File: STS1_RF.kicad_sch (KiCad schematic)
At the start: 6 parts, among them J1 Conn_Coaxial, J2 Conn_01x03_Male

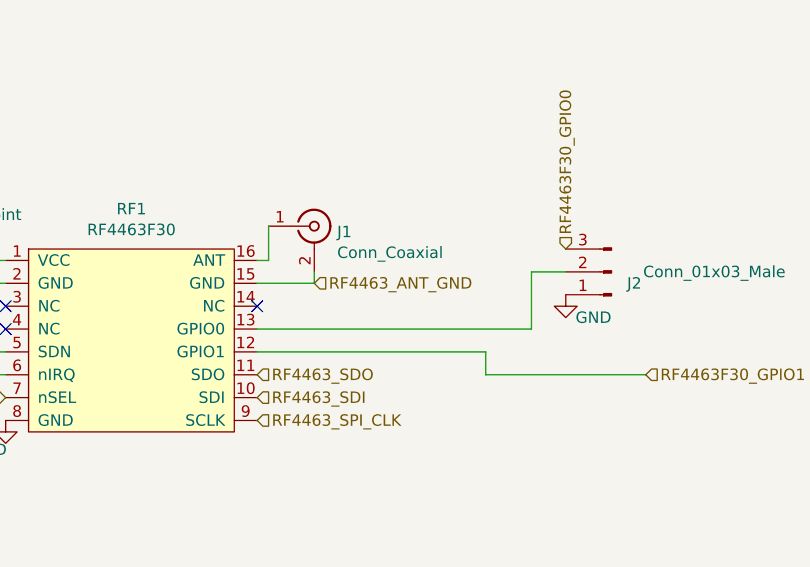
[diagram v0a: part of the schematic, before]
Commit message: more work done
All parts besides RF added
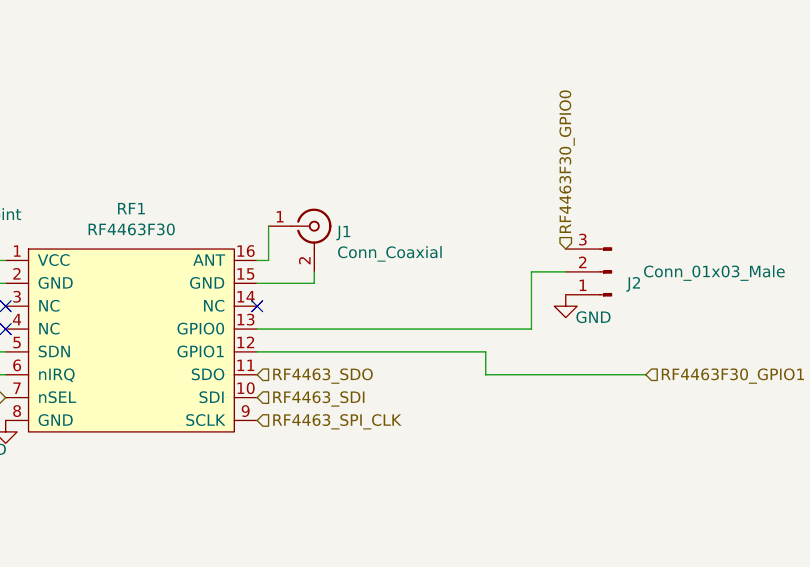
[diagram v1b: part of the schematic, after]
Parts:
- J1: footprint Connector_Coaxial:SMA_Amphenol_901-144_Vertical -> Connector_Coaxial:SMB_Jack_Vertical
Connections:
- net RF4463_ANT_GND: no longer names the net of J1.2 (Ext), RF1.15 (GND)
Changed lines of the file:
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@@
-    (effects (font (size 1.27 1.27)) (justify left))
-  )
-  (hierarchical_label "RF4463_ANT_GND" (shape input) (at 228.6 83.82 0)
     (effects (font (size 1.27 1.27)) (justify left))
   )
@@
       (effects (font (size 1.27 1.27)) (justify left))
     )
-    (property "Footprint" "Connector_Coaxial:SMA_Amphenol_901-144_Vertical" (id 2) (at 228.6 77.47 0)
+    (property "Footprint" "Connector_Coaxial:SMB_Jack_Vertical" (id 2) (at 228.6 77.47 0)
       (effects (font (size 1.27 1.27)) hide)
     )

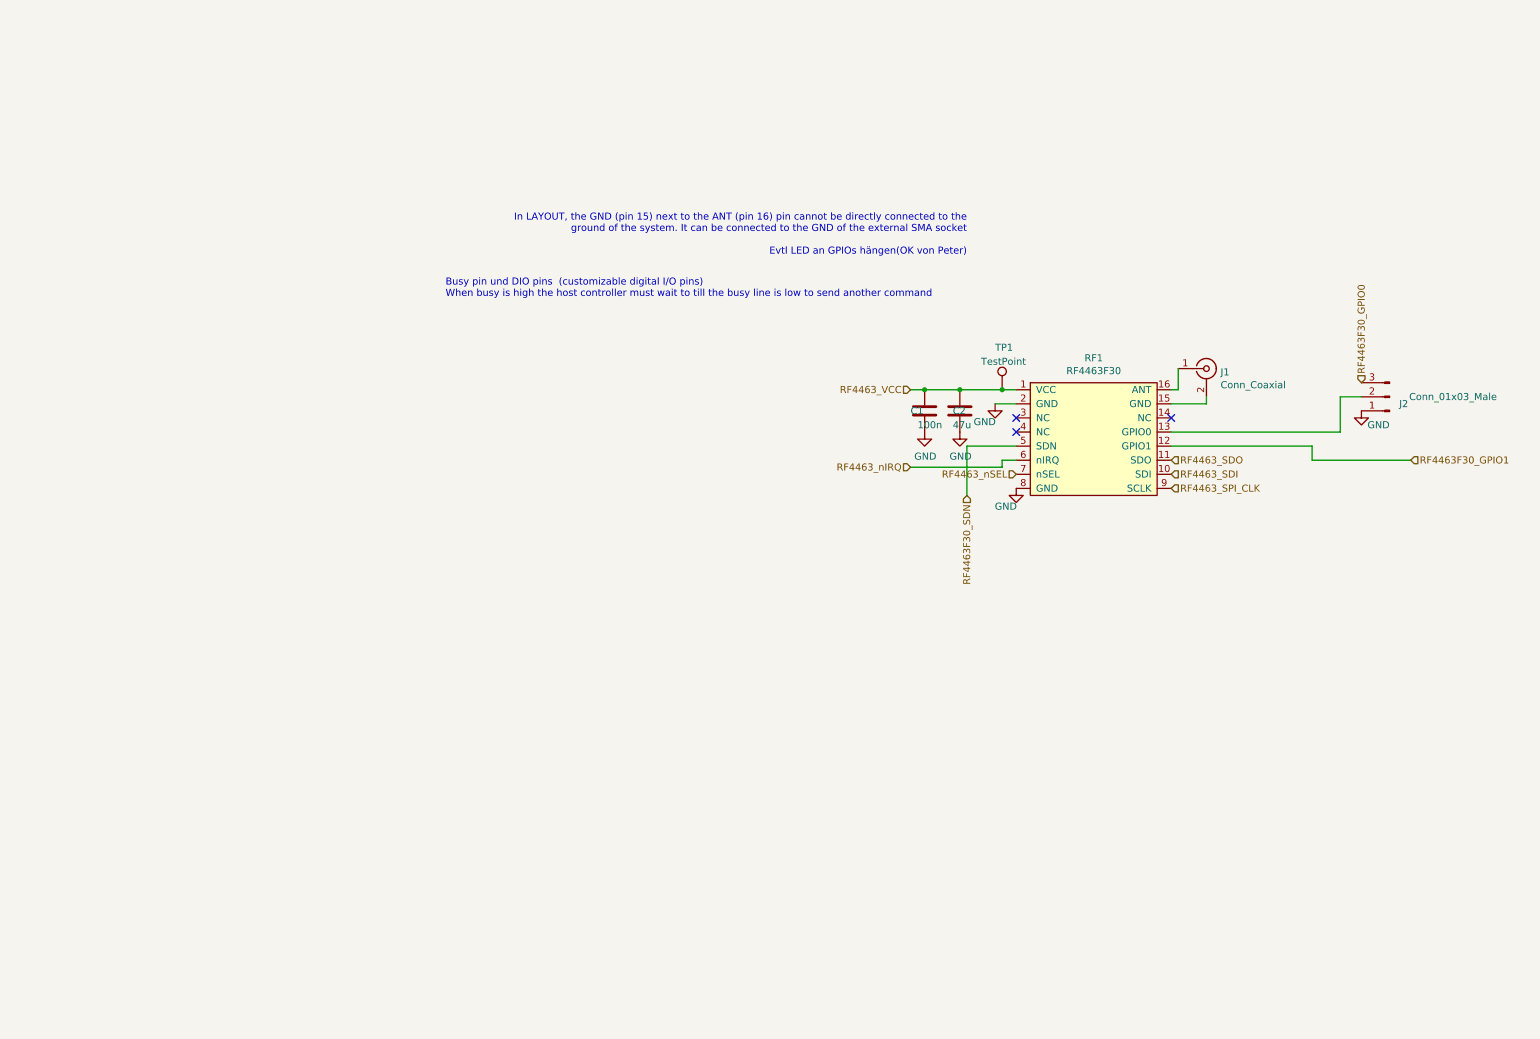
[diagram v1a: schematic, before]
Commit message: add RF part
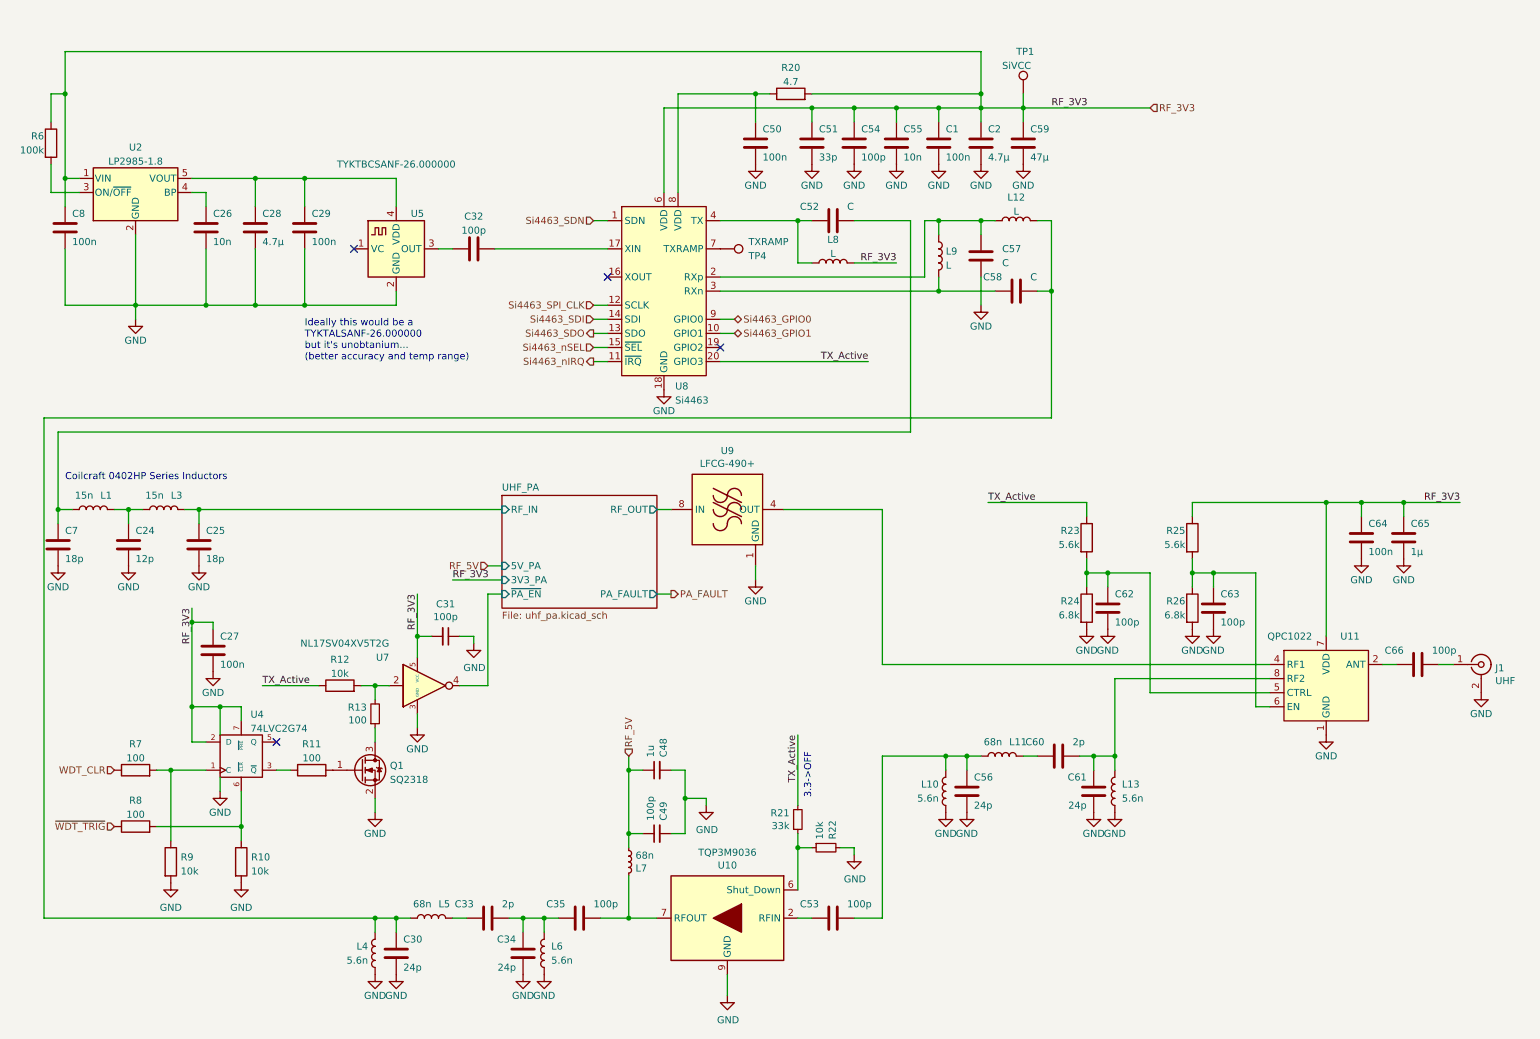
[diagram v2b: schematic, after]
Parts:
- removed J2: Conn_01x03_Male, STS1library:PinHeader_1x03_P2.54mm_Vertical_umdieEcke, symbol Connector:Conn_01x03_Male
- removed RF1: RF4463F30, STS1_RF:STS1_RF4463F30, symbol STS1_COBC_RFM:RF4463F30
- added C24: 12p, Capacitor_SMD:C_0402_1005Metric, symbol Device:C
- added C25, C7: 18p, Capacitor_SMD:C_0402_1005Metric, symbol Device:C
- added C26, C55: 10n, Capacitor_SMD:C_0805_2012Metric, symbol Device:C
- added C27, C29, C50, C64, C8: 100n, Capacitor_SMD:C_0805_2012Metric, symbol Device:C
- added C28: 4.7µ, Capacitor_SMD:C_0805_2012Metric, symbol Device:C
- added C30, C34, C56, C61: 24p, Capacitor_SMD:C_0402_1005Metric, symbol Device:C
- added C31, C49: 100p, Capacitor_SMD:C_0402_1005Metric, symbol Device:C_Small
- added C32, C35, C53, C54, C62, C63, C66: 100p, Capacitor_SMD:C_0402_1005Metric, symbol Device:C
- added C33, C60: 2p, Capacitor_SMD:C_0402_1005Metric, symbol Device:C
- added C48: 1u, Capacitor_SMD:C_0805_2012Metric, symbol Device:C_Small
- added C51: 33p, Capacitor_SMD:C_0402_1005Metric, symbol Device:C
- added C52, C57, C58: C, Capacitor_SMD:C_0402_1005Metric, symbol Device:C
- added C59: 47µ, Capacitor_SMD:C_0805_2012Metric, symbol Device:C
- added C65: 1µ, Capacitor_SMD:C_0805_2012Metric, symbol Device:C
- added L1, L3: 15n, Inductor_SMD:L_0402_1005Metric, symbol Device:L
- added L10, L13, L4, L6: 5.6n, Inductor_SMD:L_0402_1005Metric, symbol Device:L
- added L11, L5: 68n, Inductor_SMD:L_0402_1005Metric, symbol Device:L
- added L12, L8, L9: L, Inductor_SMD:L_0402_1005Metric, symbol Device:L
- added L7: 68n, Inductor_SMD:L_0402_1005Metric, symbol Device:L_Small
- added Q1: SQ2318, Package_TO_SOT_SMD:SOT-23, symbol Device:Q_NMOS_GSD
- added R10, R12, R9: 10k, Resistor_SMD:R_0603_1608Metric, symbol Device:R
- added R11, R7, R8: 100, Resistor_SMD:R_0603_1608Metric, symbol Device:R
- added R13: 100, Resistor_SMD:R_0603_1608Metric, symbol Device:R_Small
- added R20: 4.7, Resistor_SMD:R_0603_1608Metric, symbol Device:R
- added R21: 33k, Resistor_SMD:R_0603_1608Metric, symbol Device:R_Small
- added R22: 10k, Resistor_SMD:R_0603_1608Metric, symbol Device:R_Small
- added R23, R25: 5.6k, Resistor_SMD:R_0603_1608Metric, symbol Device:R
- added R24, R26: 6.8k, Resistor_SMD:R_0603_1608Metric, symbol Device:R
- added R6: 100k, Resistor_SMD:R_0603_1608Metric, symbol Device:R
- added TP4: TXRAMP, STS1library:STS1_Testpoint, symbol Connector:TestPoint
- added U10: TQP3M9036, lsf-kicad-lib:DFN-8-1EP_2x2mm_P0.5mm_EP0.7x1.6mm_ThermalVias, symbol lsf-kicad:TQP3M9036
- added U11: QPC1022, STS_Package_LGA:Qorvo_9Pin_1.1x1.5mm_LGA, symbol STS_RF_Module:QPC1022
- added U2: LP2985-1.8, Package_TO_SOT_SMD:SOT-23-5, symbol Regulator_Linear:LP2985-1.8
- added U4: 74LVC2G74, Package_SO:VSSOP-8_2.4x2.1mm_P0.5mm, symbol 74xGxx:74LVC2G74
- added U5: TYKTBCSANF-26.000000, Crystal:Crystal_SMD_2520-4Pin_2.5x2.0mm, symbol Oscillator:FT5HV
- added U7: NL17SV04XV5T2G, Package_TO_SOT_SMD:SOT-553, symbol 74xGxx:74LVC1GU04DRL
- added U8: Si4463, Package_DFN_QFN:QFN-20-1EP_4x4mm_P0.5mm_EP2.6x2.6mm_ThermalVias, symbol RF:Si4463
- added U9: LFCG-490+, lsf-kicad-lib:GE0805C-2, symbol lsf-kicad:LFCG-490+
- C2: value 47u -> 4.7µ
- J1: value Conn_Coaxial -> UHF
- TP1: value TestPoint -> SiVCC
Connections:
- net GND: now also J1.2 (Ext), C24.2, C25.2, C26.2, C27.2, C28.2, C29.2, C30.2, C31.1, C34.2, C48.2, C49.2, C50.2, C51.2, C54.2, C55.2, C56.2, C57.2, C59.2, C61.2, C62.2, C63.2, C64.2, C65.2, C7.2, C8.2, L10.1, L13.1, L4.1, L6.1, Q1.2 (S), R10.2, R22.2, R24.2, R26.2, R9.2, U10.9 (GND), U11.1 (GND), U11.3 (GND), U11.9 (GND), U2.2 (GND), U4.4 (GND), U5.2 (GND), U7.3 (GND), U8.18 (GND), U8.21 (GND), U9.1 (GND), U9.2 (GND), U9.3 (GND), U9.5 (GND), U9.6 (GND), U9.7 (GND)
- net at J1.1 (In): now also C66.2
- net RF4463_VCC renamed VCC
- net VCC: now also C27.1, C31.2, C51.1, C54.1, C55.1, C59.1, C64.1, C65.1, C8.1, L8.2, R20.2, R25.1, R6.1, U11.7 (VDD), U2.1 (VIN), U4.2 (D), U4.7 (~{PRE}), U4.8 (VCC), U7.5 (VCC), U8.6 (VDD)
- new net: R7.2, R9.1, U4.1 (C)
- new net: R12.2, R13.2, U7.2
- new net: U11.4 (RF1), U9.4 (OUT)
- new net: C50.1, R20.1, U8.8 (VDD)
- new net: TP4.1, U8.7 (TXRAMP)
- new net: C30.1, C58.2, L12.2, L4.2, L5.1
- new net: C62.1, R23.2, R24.1, U11.5 (CTRL)
- new net: C33.2, C34.1, C35.1, L6.2
- new net: C35.2, L7.1, U10.7 (RFOUT)
- new net: C24.1, L1.2, L3.1
- new net: C52.2, C7.1, L1.1
- new net: R6.2, U2.3 (ON/~{OFF})
- new net: R21.1, R22.1, U10.6 (Shut_Down)
- new net: C33.1, L5.2
- new net: C28.1, C29.1, U2.5 (VOUT), U5.4 (VDD)
- new net: C63.1, R25.2, R26.1, U11.6 (EN)
- new net: R11.1, U4.3 (~{Q})
- new net: R10.1, R8.2, U4.6 (~{CLR})
- new net: Q1.3 (D), R13.1
- new net: C60.1, L11.2
- new net: C60.2, C61.1, L13.2, U11.8 (RF2)
- new net: C52.1, L8.1, U8.4 (TX)
- new net: C53.2, C56.1, L10.2, L11.1
- new net: C53.1, U10.2 (RFIN)
- new net: C57.1, L12.1, L9.1, U8.2 (RXp)
- new net: C32.1, U5.3 (OUT)
- new net: C32.2, U8.17 (XIN)
- new net: C58.1, L9.2, U8.3 (RXn)
- new net: C26.1, U2.4 (BP)
- new net: C66.1, U11.2 (ANT)
- new net: Q1.1 (G), R11.2
- new net RF_5V: C48.1, C49.1, L7.2
- new net Si4463_GPIO0: U8.9 (GPIO0)
- new net Si4463_GPIO1: U8.10 (GPIO1)
- new net Si4463_SDI: U8.14 (SDI)
- new net Si4463_SDN: U8.1 (SDN)
- new net Si4463_SDO: U8.13 (SDO)
- new net Si4463_SPI_CLK: U8.12 (SCLK)
- new net Si4463_nIRQ: U8.11 (~{IRQ})
- new net Si4463_nSEL: U8.15 (~{SEL})
- new net TX_Active: R12.1, R21.2, R23.1, U8.20 (GPIO3)
- new net UHF_PA/RF_IN: C25.1, L3.2
- new net UHF_PA/RF_OUT: U9.8 (IN)
- new net UHF_PA/~{PA_EN}: U7.4
- new net WDT_CLR: R7.1
- new net ~{WDT_TRIG}: R8.1
- no-connect marks 3 -> 4
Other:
- added sheet UHF_PA (uhf_pa.kicad_sch)
- note added: "3.3->OFF"
- note added: "Coilcraft 0402HP Series Inductors"
- note added: "Ideally this would be a TYKTALSANF-26.000000 but it's unobtanium... (better accuracy and temp range)"
- note removed: "Busy pin und DIO pins (customizable digital I/O pins) When busy is high the host controller must wait to till the busy line is low to send another command"
- note removed: "In LAYOUT, the GND (pin 15) next to the ANT (pin 16) pin cannot be directly connected to the ground of the system. It can be connected to the GND of the external SMA socket Evtl LED an GPIOs hängen(OK von Peter)"
- moved on the sheet: C1, C2, J1, TP1

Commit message: add values for si4463 input matching network
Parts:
- C52: value C -> 8.2p
- C57: value C -> 3.9p
- C58: value C -> 2.2p
- L12: value L -> 51n
- L8: value L -> 220n
- L9: value L -> 56n
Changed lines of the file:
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@@
     (in_bom yes) (on_board yes)
     (property "Reference" "L8" (id 0) (at 161.29 54.2122 90))
-    (property "Value" "L" (id 1) (at 161.29 56.7491 90))
+    (property "Value" "220n" (id 1) (at 161.29 56.7491 90))
     (property "Footprint" "Inductor_SMD:L_0402_1005Metric" (id 2) (at 161.29 58.42 0)
       (effects (font (size 1.27 1.27)) hide)
@@
       (effects (font (size 1.27 1.27)) (justify left))
     )
-    (property "Value" "C" (id 1) (at 191.77 58.42 0)
+    (property "Value" "3.9p" (id 1) (at 191.77 58.42 0)
       (effects (font (size 1.27 1.27)) (justify left))
     )
@@
       (effects (font (size 1.27 1.27)) (justify left))
     )
-    (property "Value" "C" (id 1) (at 163.83 48.26 90)
+    (property "Value" "8.2p" (id 1) (at 163.83 48.26 90)
       (effects (font (size 1.27 1.27)) (justify right))
     )
@@
       (effects (font (size 1.27 1.27)) (justify left))
     )
-    (property "Value" "L" (id 1) (at 181.61 58.8522 0)
+    (property "Value" "56n" (id 1) (at 181.61 58.8522 0)
       (effects (font (size 1.27 1.27)) (justify left))
     )
@@
       (effects (font (size 1.27 1.27)) (justify left))
     )
-    (property "Value" "C" (id 1) (at 196.85 60.96 90)
+    (property "Value" "2.2p" (id 1) (at 196.85 60.96 90)
       (effects (font (size 1.27 1.27)) (justify right))
     )
@@
     (in_bom yes) (on_board yes)
     (property "Reference" "L12" (id 0) (at 194.31 46.5922 90))
-    (property "Value" "L" (id 1) (at 194.31 49.1291 90))
+    (property "Value" "51n" (id 1) (at 194.31 49.1291 90))
     (property "Footprint" "Inductor_SMD:L_0402_1005Metric" (id 2) (at 194.31 50.8 0)
       (effects (font (size 1.27 1.27)) hide)

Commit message: Remove old submodules
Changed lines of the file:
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@@
     (pin "2")
+  )
+  (symbol (lib_id "power:PWR_FLAG") (at 133.35 27.94 0) (unit 1)
+    (in_bom yes) (on_board yes) (fields_autoplaced)
+    (property "Reference" "#FLG01" (id 0) (at 133.35 26.035 0)
+      (effects (font (size 1.27 1.27)) hide)
+    )
+    (property "Value" "PWR_FLAG" (id 1) (at 133.35 22.86 0))
+    (property "Footprint" "" (id 2) (at 133.35 27.94 0)
+      (effects (font (size 1.27 1.27)) hide)
+    )
+    (property "Datasheet" "~" (id 3) (at 133.35 27.94 0)
+      (effects (font (size 1.27 1.27)) hide)
+    )
+    (pin "1")
   )
   (symbol (lib_id "Device:L") (at 212.09 153.67 180) (unit 1)
